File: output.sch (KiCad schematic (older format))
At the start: 6 parts

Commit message: Netlist and PCB generated
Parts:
- P14, P15, P16, P17, P18, P19: renamed from P?; footprint (none) -> Pin_Headers:Pin_Header_Straight_1x03
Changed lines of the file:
@@
 $EndDescr
 $Comp
-L CONN_01X03 P?
+L CONN_01X03 P14
 U 1 1 57FDB1CC
 P 2250 1250
-F 0 "P?" H 2250 1450 50  0000 C CNN
+F 0 "P14" H 2250 1450 50  0000 C CNN
 F 1 "SERVO_OUT_0" V 2350 1250 50  0000 C CNN
-F 2 "" H 2250 1250 50  0000 C CNN
+F 2 "Pin_Headers:Pin_Header_Straight_1x03" H 2250 1250 50  0001 C CNN
 F 3 "" H 2250 1250 50  0000 C CNN
 	1    2250 1250
@@
 	1900 1150 2050 1150
 $Comp
-L +5V #PWR?
+L +5V #PWR02
 U 1 1 57FDC07E
 P 2000 1050
-F 0 "#PWR?" H 2000 900 50  0001 C CNN
+F 0 "#PWR02" H 2000 900 50  0001 C CNN
 F 1 "+5V" H 2000 1190 50  0000 C CNN
 F 2 "" H 2000 1050 50  0000 C CNN
@@
 $EndComp
 $Comp
-L GND #PWR?
+L GND #PWR03
 U 1 1 57FDC0EB
 P 2000 1400
-F 0 "#PWR?" H 2000 1150 50  0001 C CNN
+F 0 "#PWR03" H 2000 1150 50  0001 C CNN
 F 1 "GND" H 2000 1250 50  0000 C CNN
 F 2 "" H 2000 1400 50  0000 C CNN
@@
 	2000 1250 2000 1050
 $Comp
-L CONN_01X03 P?
+L CONN_01X03 P15
 U 1 1 57FDC48B
 P 2250 2050
-F 0 "P?" H 2250 2250 50  0000 C CNN
+F 0 "P15" H 2250 2250 50  0000 C CNN
 F 1 "SERVO_OUT_1" V 2350 2050 50  0000 C CNN
-F 2 "" H 2250 2050 50  0000 C CNN
+F 2 "Pin_Headers:Pin_Header_Straight_1x03" H 2250 2050 50  0001 C CNN
 F 3 "" H 2250 2050 50  0000 C CNN
 	1    2250 2050
@@
 	1900 1950 2050 1950
 $Comp
-L +5V #PWR?
+L +5V #PWR04
 U 1 1 57FDC493
 P 2000 1850
-F 0 "#PWR?" H 2000 1700 50  0001 C CNN
+F 0 "#PWR04" H 2000 1700 50  0001 C CNN
 F 1 "+5V" H 2000 1990 50  0000 C CNN
 F 2 "" H 2000 1850 50  0000 C CNN
@@
 $EndComp
 $Comp
-L GND #PWR?
+L GND #PWR05
 U 1 1 57FDC499
 P 2000 2200
-F 0 "#PWR?" H 2000 1950 50  0001 C CNN
+F 0 "#PWR05" H 2000 1950 50  0001 C CNN
 F 1 "GND" H 2000 2050 50  0000 C CNN
 F 2 "" H 2000 2200 50  0000 C CNN
@@
 	2000 2050 2000 1850
 $Comp
-L CONN_01X03 P?
+L CONN_01X03 P16
 U 1 1 57FDC599
 P 2250 2800
-F 0 "P?" H 2250 3000 50  0000 C CNN
+F 0 "P16" H 2250 3000 50  0000 C CNN
 F 1 "SERVO_OUT_2" V 2350 2800 50  0000 C CNN
-F 2 "" H 2250 2800 50  0000 C CNN
+F 2 "Pin_Headers:Pin_Header_Straight_1x03" H 2250 2800 50  0001 C CNN
 F 3 "" H 2250 2800 50  0000 C CNN
 	1    2250 2800
@@
 	1900 2700 2050 2700
 $Comp
-L +5V #PWR?
+L +5V #PWR06
 U 1 1 57FDC5A1
 P 2000 2600
-F 0 "#PWR?" H 2000 2450 50  0001 C CNN
+F 0 "#PWR06" H 2000 2450 50  0001 C CNN
 F 1 "+5V" H 2000 2740 50  0000 C CNN
 F 2 "" H 2000 2600 50  0000 C CNN
@@
 $EndComp
 $Comp
-L GND #PWR?
+L GND #PWR07
 U 1 1 57FDC5A7
 P 2000 2950
-F 0 "#PWR?" H 2000 2700 50  0001 C CNN
+F 0 "#PWR07" H 2000 2700 50  0001 C CNN
 F 1 "GND" H 2000 2800 50  0000 C CNN
 F 2 "" H 2000 2950 50  0000 C CNN
@@
 	2000 2800 2000 2600
 $Comp
-L CONN_01X03 P?
+L CONN_01X03 P17
 U 1 1 57FDC5B1
 P 2250 3600
-F 0 "P?" H 2250 3800 50  0000 C CNN
+F 0 "P17" H 2250 3800 50  0000 C CNN
 F 1 "SERVO_OUT_3" V 2350 3600 50  0000 C CNN
-F 2 "" H 2250 3600 50  0000 C CNN
+F 2 "Pin_Headers:Pin_Header_Straight_1x03" H 2250 3600 50  0001 C CNN
 F 3 "" H 2250 3600 50  0000 C CNN
 	1    2250 3600
@@
 	1900 3500 2050 3500
 $Comp
-L +5V #PWR?
+L +5V #PWR08
 U 1 1 57FDC5B9
 P 2000 3400
-F 0 "#PWR?" H 2000 3250 50  0001 C CNN
+F 0 "#PWR08" H 2000 3250 50  0001 C CNN
 F 1 "+5V" H 2000 3540 50  0000 C CNN
 F 2 "" H 2000 3400 50  0000 C CNN
@@
 $EndComp
 $Comp
-L GND #PWR?
+L GND #PWR09
 U 1 1 57FDC5BF
 P 2000 3750
-F 0 "#PWR?" H 2000 3500 50  0001 C CNN
+F 0 "#PWR09" H 2000 3500 50  0001 C CNN
 F 1 "GND" H 2000 3600 50  0000 C CNN
 F 2 "" H 2000 3750 50  0000 C CNN
@@
 	2000 3600 2000 3400
 $Comp
-L CONN_01X03 P?
+L CONN_01X03 P18
 U 1 1 57FDC653
 P 2250 4350
-F 0 "P?" H 2250 4550 50  0000 C CNN
+F 0 "P18" H 2250 4550 50  0000 C CNN
 F 1 "SERVO_OUT_4" V 2350 4350 50  0000 C CNN
-F 2 "" H 2250 4350 50  0000 C CNN
+F 2 "Pin_Headers:Pin_Header_Straight_1x03" H 2250 4350 50  0001 C CNN
 F 3 "" H 2250 4350 50  0000 C CNN
 	1    2250 4350
@@
 	1900 4250 2050 4250
 $Comp
-L +5V #PWR?
+L +5V #PWR010
 U 1 1 57FDC65B
 P 2000 4150
-F 0 "#PWR?" H 2000 4000 50  0001 C CNN
+F 0 "#PWR010" H 2000 4000 50  0001 C CNN
 F 1 "+5V" H 2000 4290 50  0000 C CNN
 F 2 "" H 2000 4150 50  0000 C CNN
@@
 $EndComp
 $Comp
-L GND #PWR?
+L GND #PWR011
 U 1 1 57FDC661
 P 2000 4500
-F 0 "#PWR?" H 2000 4250 50  0001 C CNN
+F 0 "#PWR011" H 2000 4250 50  0001 C CNN
 F 1 "GND" H 2000 4350 50  0000 C CNN
 F 2 "" H 2000 4500 50  0000 C CNN
@@
 	2000 4350 2000 4150
 $Comp
-L CONN_01X03 P?
+L CONN_01X03 P19
 U 1 1 57FDC66B
 P 2250 5150
-F 0 "P?" H 2250 5350 50  0000 C CNN
+F 0 "P19" H 2250 5350 50  0000 C CNN
 F 1 "SERVO_OUT_5" V 2350 5150 50  0000 C CNN
-F 2 "" H 2250 5150 50  0000 C CNN
+F 2 "Pin_Headers:Pin_Header_Straight_1x03" H 2250 5150 50  0001 C CNN
 F 3 "" H 2250 5150 50  0000 C CNN
 	1    2250 5150
@@
 	1900 5050 2050 5050
 $Comp
-L +5V #PWR?
+L +5V #PWR012
 U 1 1 57FDC673
 P 2000 4950
-F 0 "#PWR?" H 2000 4800 50  0001 C CNN
+F 0 "#PWR012" H 2000 4800 50  0001 C CNN
 F 1 "+5V" H 2000 5090 50  0000 C CNN
 F 2 "" H 2000 4950 50  0000 C CNN
@@
 $EndComp
 $Comp
-L GND #PWR?
+L GND #PWR013
 U 1 1 57FDC679
 P 2000 5300
-F 0 "#PWR?" H 2000 5050 50  0001 C CNN
+F 0 "#PWR013" H 2000 5050 50  0001 C CNN
 F 1 "GND" H 2000 5150 50  0000 C CNN
 F 2 "" H 2000 5300 50  0000 C CNN

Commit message: PCB rev1.0
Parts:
- added P9: PWR_OUT, Socket_Strips:Socket_Strip_Straight_1x02, symbol CONN_01X02
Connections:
- net +5V: now also P9.1 (P1); no longer P14.2 (P2), P15.2 (P2), P16.2 (P2), P17.2 (P2), P18.2 (P2), P19.2 (P2)
- net GND: now also P9.2 (P2)
- new net 5V_SERVO: P14.2 (P2), P15.2 (P2), P16.2 (P2), P17.2 (P2), P18.2 (P2), P19.2 (P2)
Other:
- moved on the sheet: P15, P16, P17, P18, P19

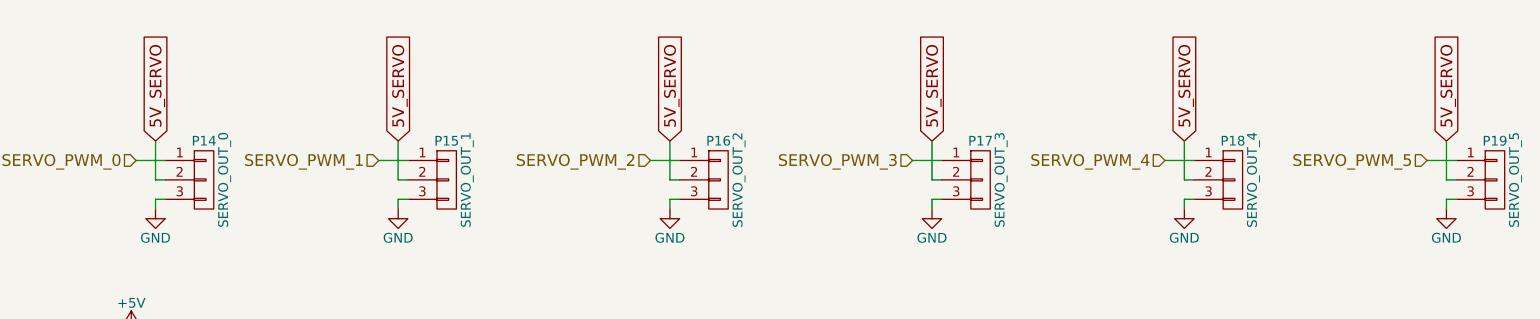
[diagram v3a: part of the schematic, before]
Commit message: Jumper removed, pdf generated
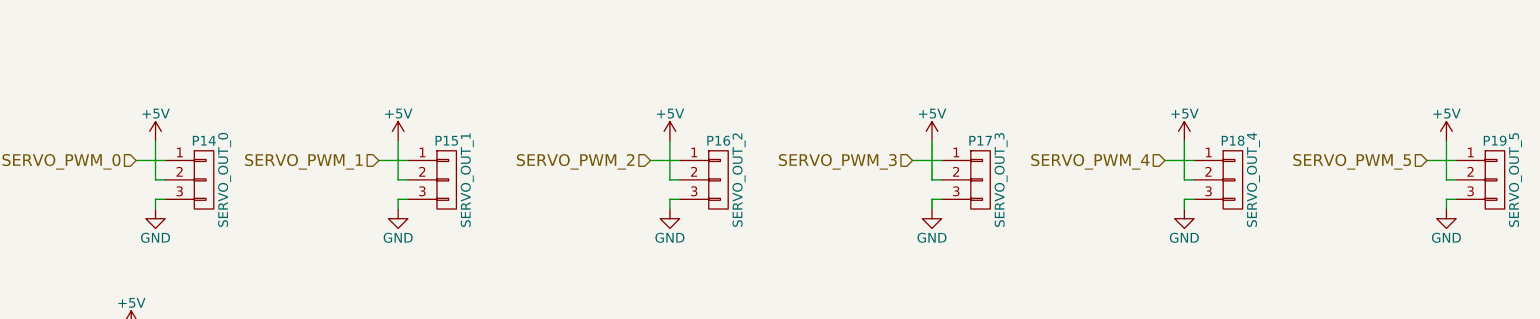
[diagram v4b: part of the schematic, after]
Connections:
- net 5V_SERVO is gone; now on net +5V: P14.2 (P2), P15.2 (P2), P16.2 (P2), P17.2 (P2), P18.2 (P2), P19.2 (P2)
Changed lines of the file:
@@
 Wire Wire Line
 	8650 1250 8650 1050
-Text GLabel 2000 1050 1    60   Input ~ 0
-5V_SERVO
-Text GLabel 3250 1050 1    60   Input ~ 0
-5V_SERVO
-Text GLabel 4650 1050 1    60   Input ~ 0
-5V_SERVO
-Text GLabel 6000 1050 1    60   Input ~ 0
-5V_SERVO
-Text GLabel 7300 1050 1    60   Input ~ 0
-5V_SERVO
-Text GLabel 8650 1050 1    60   Input ~ 0
-5V_SERVO
 $Comp
 L CONN_01X02 P9
@@
 Wire Wire Line
 	1875 2125 1875 2025
+$Comp
+L +5V #PWR?
+U 1 1 58024124
+P 2000 1050
+F 0 "#PWR?" H 2000 900 50  0001 C CNN
+F 1 "+5V" H 2000 1190 50  0000 C CNN
+F 2 "" H 2000 1050 50  0000 C CNN
+F 3 "" H 2000 1050 50  0000 C CNN
+	1    2000 1050
+	1    0    0    -1
+$EndComp
+$Comp
+L +5V #PWR?
+U 1 1 58024144
+P 3250 1050
+F 0 "#PWR?" H 3250 900 50  0001 C CNN
+F 1 "+5V" H 3250 1190 50  0000 C CNN
+F 2 "" H 3250 1050 50  0000 C CNN
+F 3 "" H 3250 1050 50  0000 C CNN
+	1    3250 1050
+	1    0    0    -1
+$EndComp
+$Comp
+L +5V #PWR?
+U 1 1 58024164
+P 4650 1050
+F 0 "#PWR?" H 4650 900 50  0001 C CNN
+F 1 "+5V" H 4650 1190 50  0000 C CNN
+F 2 "" H 4650 1050 50  0000 C CNN
+F 3 "" H 4650 1050 50  0000 C CNN
+	1    4650 1050
+	1    0    0    -1
+$EndComp
+$Comp
+L +5V #PWR?
+U 1 1 58024184
+P 6000 1050
+F 0 "#PWR?" H 6000 900 50  0001 C CNN
+F 1 "+5V" H 6000 1190 50  0000 C CNN
+F 2 "" H 6000 1050 50  0000 C CNN
+F 3 "" H 6000 1050 50  0000 C CNN
+	1    6000 1050
+	1    0    0    -1
+$EndComp
+$Comp
+L +5V #PWR?
+U 1 1 580241F8
+P 7300 1050
+F 0 "#PWR?" H 7300 900 50  0001 C CNN
+F 1 "+5V" H 7300 1190 50  0000 C CNN
+F 2 "" H 7300 1050 50  0000 C CNN
+F 3 "" H 7300 1050 50  0000 C CNN
+	1    7300 1050
+	1    0    0    -1
+$EndComp
+$Comp
+L +5V #PWR?
+U 1 1 58024218
+P 8650 1050
+F 0 "#PWR?" H 8650 900 50  0001 C CNN
+F 1 "+5V" H 8650 1190 50  0000 C CNN
+F 2 "" H 8650 1050 50  0000 C CNN
+F 3 "" H 8650 1050 50  0000 C CNN
+	1    8650 1050
+	1    0    0    -1
+$EndComp
 $EndSCHEMATC
